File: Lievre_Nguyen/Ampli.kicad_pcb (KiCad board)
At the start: 2 copper layers, 52 parts, among them J2 Conn_01x02, J3 Conn_01x03, Q1 2N2907, Q10 TIP32, Q11 BD138, Q12 TIP31, Q13 2N2222, Q2 2N2907, Q3 2N2907, Q4 2N2222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

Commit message: Fin du routage
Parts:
- U1: value Relay_1CT -> Relay1_Relay_1CT
- moved C8 38.6 mm to (143.5, 82.5), turned to 0 degrees
- moved C9 21.3 mm to (134.6, 91.4), turned to 0 degrees
- moved Q9 20.5 mm to (116.8, 94.0), turned to 270 degrees
- moved HS1 12.7 mm to (121.9, 82.5)
- moved Q10 9.25 mm to (123.2, 92.7), turned to 90 degrees
- moved R8 2.54 mm to (87.6, 85.1)
- moved RV1 2.54 mm to (99.1, 87.6)
- moved U2 1.27 mm to (86.4, 135.9)
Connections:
- C5 pad 2: Net-(C5-Pad2) -> GND
- C7 pad 1: Net-(C5-Pad2) -> GND
- J3 pad 2: Net-(C5-Pad2) -> GND
- Q2 pad 2: -12V -> Net-(Q2-Pad2)
- R14 pad 1: -12V -> Net-(Q2-Pad2)
- R15 pad 1: -12V -> Net-(Q2-Pad2)
- R7 pad 2: Net-(Q6-Pad1) -> Net-(R7-Pad2)
- R9 pad 2: Net-(Q7-Pad1) -> Net-(R9-Pad2)
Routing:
- net +12V: track 0.00 -> 257.7 mm
- net -12V: track 0.00 -> 202.9 mm
- net Net-(R11-Pad2): track 0.00 -> 143.2 mm
- net Net-(C2-Pad1): track 0.00 -> 65.5 mm
- net Net-(Q2-Pad2): track 0.00 -> 53.0 mm
- net Net-(C2-Pad2): track 0.00 -> 45.8 mm
- net Net-(Q1-Pad1): track 0.00 -> 45.5 mm
- net Net-(Q6-Pad3): track 0.10 -> 43.3 mm
- net Net-(Q11-Pad2): track 0.00 -> 39.4 mm
- net Net-(Q2-Pad3): track 0.00 -> 38.8 mm
- net Net-(Q6-Pad1): track 0.00 -> 36.4 mm
- net Net-(C3-Pad1): track 0.00 -> 36.0 mm
- net Net-(D1-Pad2): track 0.00 -> 29.6 mm
- net Net-(Q10-Pad3): track 0.00 -> 29.2 mm
- net Net-(C1-Pad1): track 0.00 -> 28.9 mm
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- added copper zone on B.Cu, net GND
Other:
- board text added: "LIEVRE/NGUYEN 25/04/20 PCB BOTTOM"

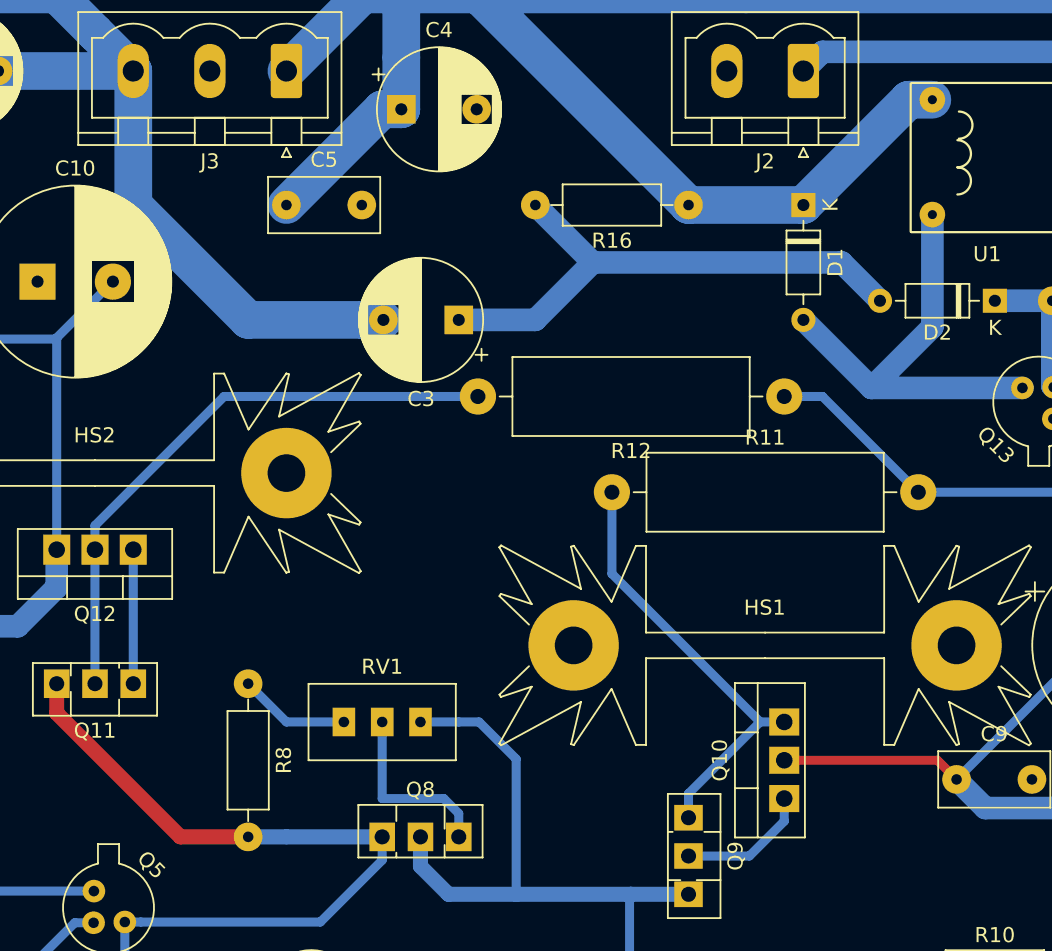
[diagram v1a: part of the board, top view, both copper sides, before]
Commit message: Fin du routage Résolution de quelques petites erreurs
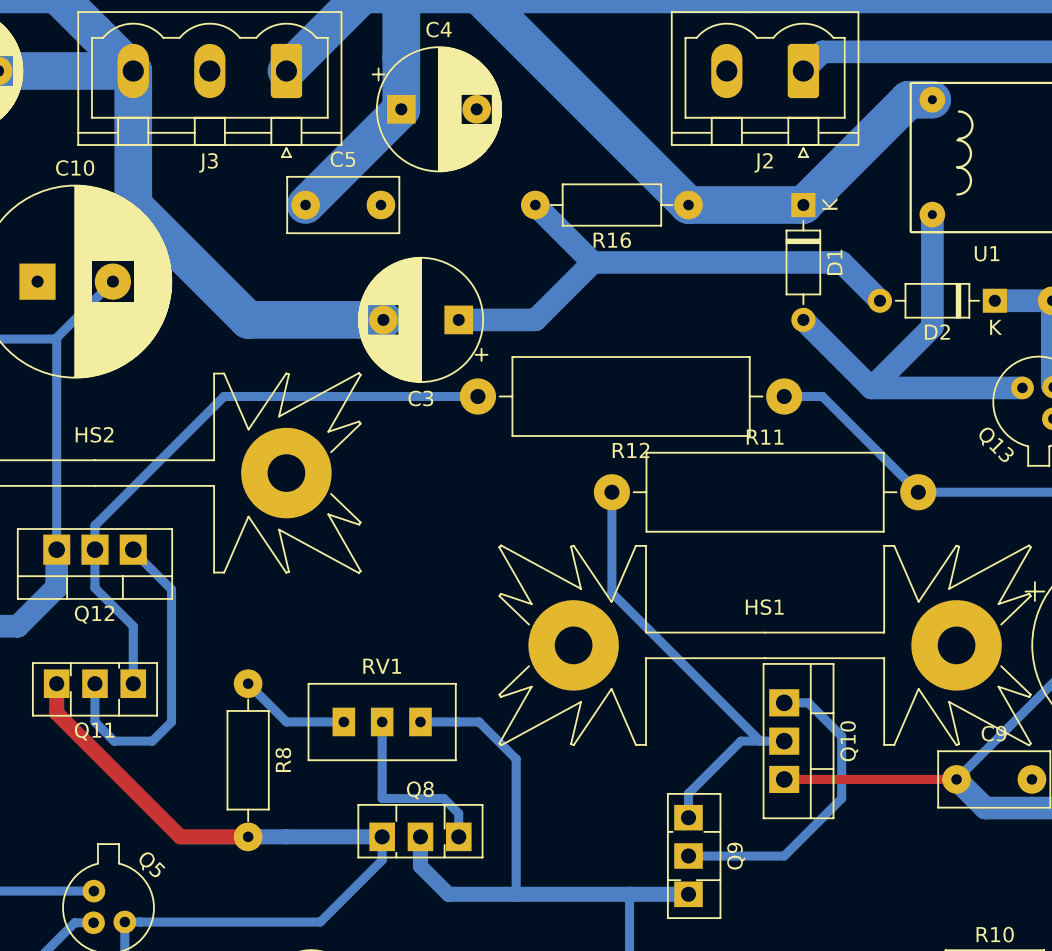
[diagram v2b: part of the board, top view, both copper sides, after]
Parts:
- moved Q10 6.35 mm to (123.2, 86.4), turned to 270 degrees
- moved C5 1.27 mm to (91.4, 53.3)
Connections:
- Q10 pad 2: +12V -> Net-(Q10-Pad2)
- Q10 pad 3: Net-(Q10-Pad3) -> +12V
- Q12 pad 1: Net-(Q11-Pad1) -> Net-(Q11-Pad2)
- Q12 pad 2: Net-(Q11-Pad2) -> Net-(Q11-Pad1)
- Q9 pad 1: Net-(Q10-Pad3) -> Net-(Q10-Pad2)
- R11 pad 1: Net-(Q10-Pad3) -> Net-(Q10-Pad2)
- R12 pad 2: Net-(Q11-Pad2) -> Net-(Q11-Pad1)
- R7 pad 2: Net-(R7-Pad2) -> Net-(Q6-Pad1)
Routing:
- net Net-(Q11-Pad1): track 8.89 -> 40.5 mm
- net Net-(Q10-Pad2): track 0.00 -> 30.0 mm
- net Net-(Q10-Pad3): track 29.2 -> 0.00 mm
- net Net-(Q11-Pad2): track 39.4 -> 21.2 mm
- net Net-(Q10-Pad1): track 8.81 -> 20.6 mm
- net +12V: track 257.7 -> 255.9 mm

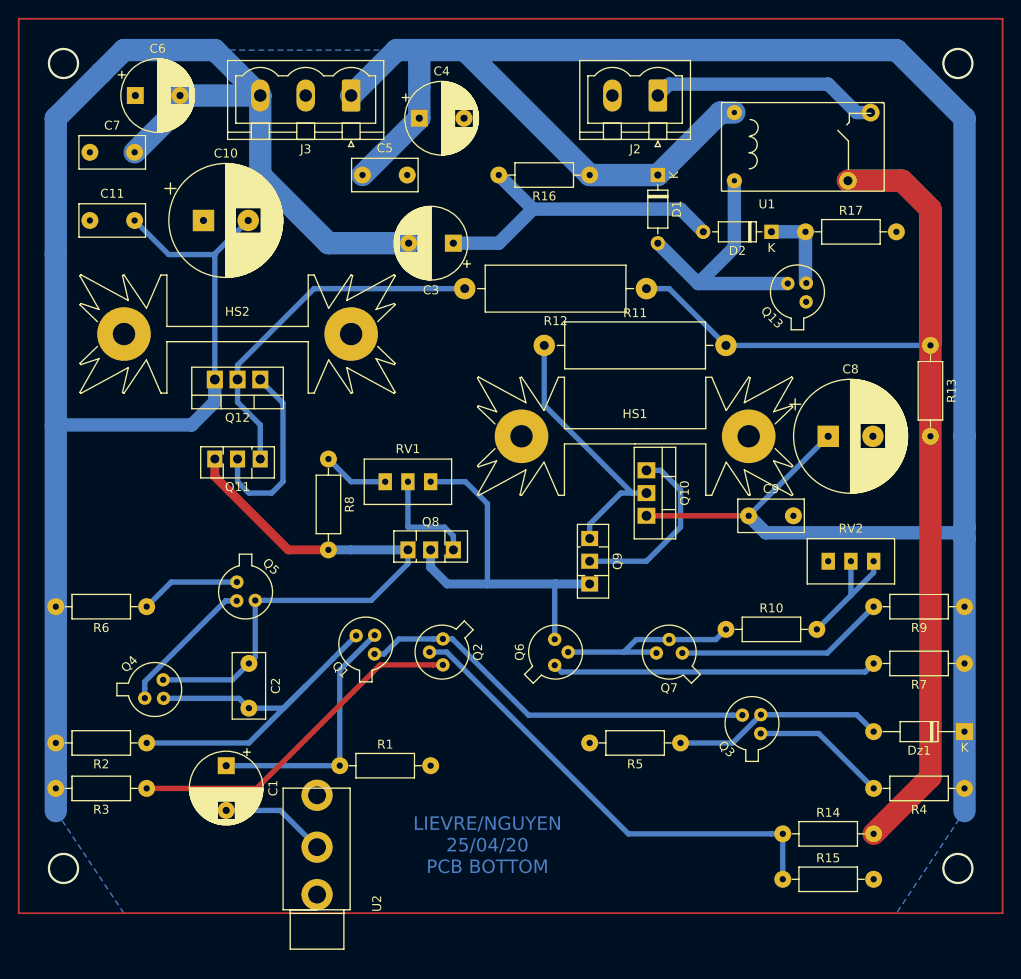
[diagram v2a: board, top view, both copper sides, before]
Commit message: Correction des erreurs sauf erreur 'bornier d'enceinte (sortie)'
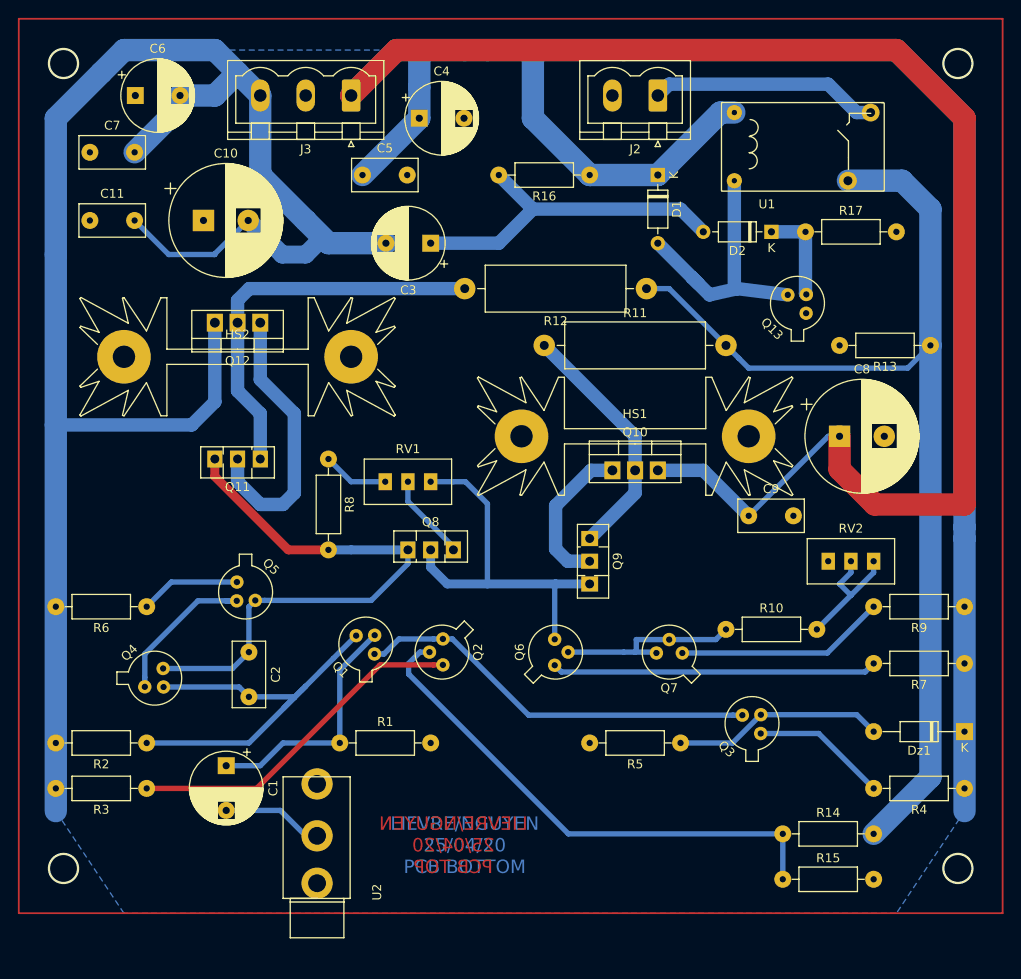
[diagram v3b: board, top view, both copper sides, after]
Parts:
- moved Q12 6.35 mm to (80.0, 69.8)
- moved Q10 3.81 mm to (119.4, 86.4), turned to 0 degrees
- moved C3 2.54 mm to (99.1, 61.0)
- moved HS2 2.54 mm to (77.5, 73.7)
- moved R1 2.54 mm to (88.9, 116.8)
- moved C8 1.27 mm to (144.8, 82.5)
- moved Q4 1.27 mm to (67.3, 110.5)
- moved C2 1.27 mm to (78.7, 106.7)
- moved Q13 1.27 mm to (141.0, 68.6)
- moved U2 1.27 mm to (86.4, 134.6)
- turned R13 to 180 degrees
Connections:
- R9 pad 2: Net-(R9-Pad2) -> Net-(Q7-Pad1)
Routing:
- net +12V: track 255.9 -> 366.0 mm
- net Net-(R11-Pad2): track 143.2 -> 119.5 mm
- net Net-(Q11-Pad2): track 21.2 -> 31.2 mm
- net Net-(Q2-Pad2): track 53.0 -> 58.4 mm
- net Net-(Q11-Pad1): track 40.5 -> 44.8 mm
- net Net-(Q10-Pad1): track 20.6 -> 17.3 mm
- net Net-(Q4-Pad1): track 15.9 -> 18.4 mm
- net Net-(C3-Pad1): track 36.0 -> 38.5 mm
- net Net-(Q8-Pad3): track 12.2 -> 9.82 mm
- net Net-(Q10-Pad2): track 30.0 -> 27.9 mm
- net -12V: track 202.9 -> 201.0 mm
- net Net-(C1-Pad1): track 28.9 -> 27.4 mm
- net Net-(D2-Pad1): track 9.58 -> 10.9 mm
- net Net-(C2-Pad1): track 65.5 -> 64.2 mm
- net Net-(C2-Pad2): track 45.8 -> 47.0 mm
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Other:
- net class Default: clearance 0.2 -> 0.3; trace_width 0.25 -> 0.4; via_dia 0.8 -> 1.9; via_drill 0.4 -> 0.6
- rule trace_clearance: 0.2 -> 0.3
- rule trace_min: 0.2 -> 0.4
- rule via_min_size: 0.4 -> 1.9
- board text added: "LIEVRE/NGUYEN 25/04/20 PCB TOP"
